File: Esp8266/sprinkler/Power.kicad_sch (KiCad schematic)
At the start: 54 parts, among them Q1 AO4407A, Q2 MMBT2222A, Q3 AON7410, U1 MAX1873TEEE, U2 TPS5410DR, U3 PC817, U4 LM2577S-ADJ_NOPB

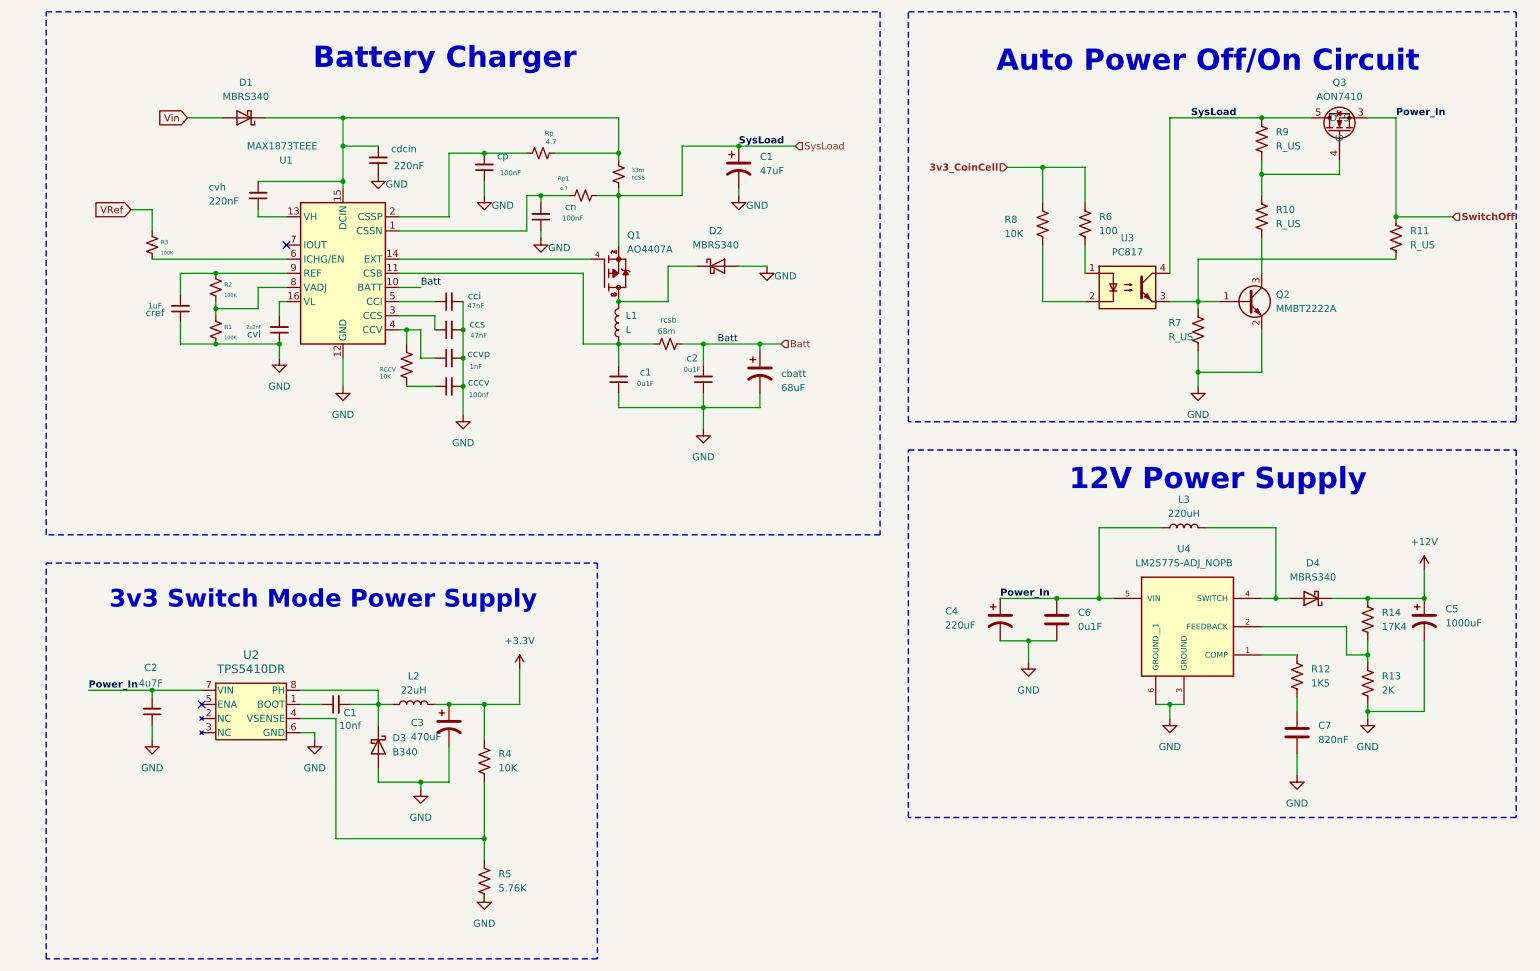
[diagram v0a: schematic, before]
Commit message: Sprinklers
Added RTC and valver drivers modules for the Sprinklers
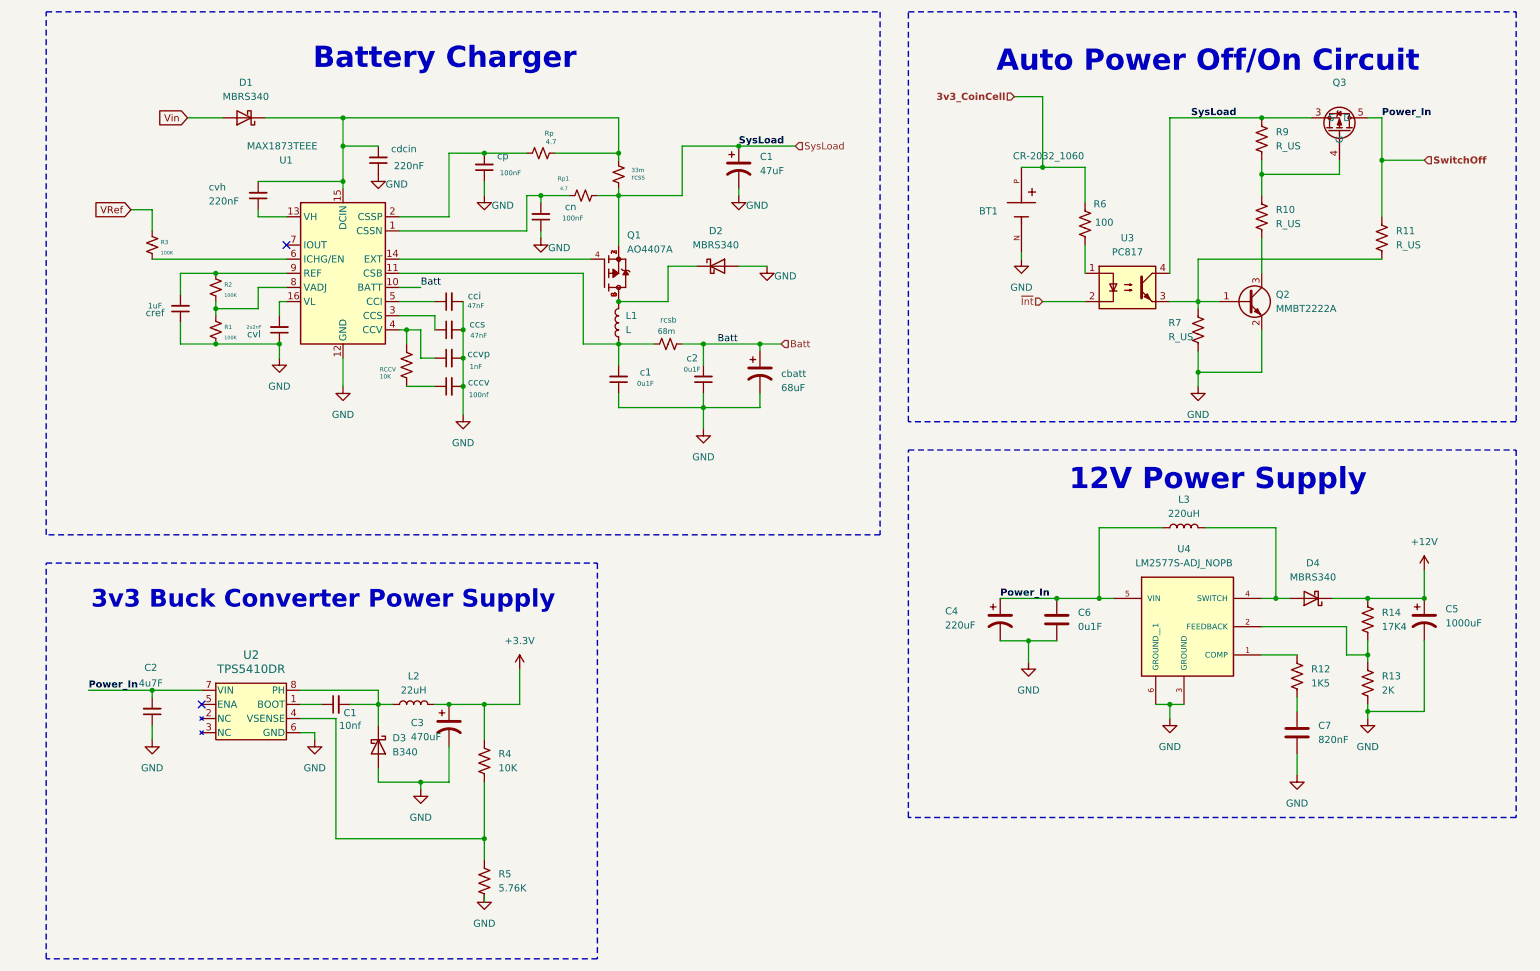
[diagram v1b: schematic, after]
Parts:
- removed Q3: AON7410, Local_Footprints:DFN_3X3_EP, symbol _Misc_Symbols:AON7410
- removed R8: 10K, symbol Device:R_US
- added BT1: CR-2032_1060, User_Footprint:BAT_1060, symbol _Misc_Symbols:CR-2032_1060
- added Q3: ~, User_Footprint:DFN_3X3_EP, symbol _Misc_Symbols:AON7401
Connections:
- net 3v3_CoinCell: now also BT1.P
- net GND: now also BT1.N
- net SwitchOff: now also Q3.5 (D), Q3.6 (D), Q3.7 (D), Q3.8 (D)
- net SysLoad: now also Q3.3 (S)
- net ~{Int}: now reaches U3.2
- net at R10.1, R9.2: now also Q3.4 (G)
- new net: Q3.1 (S), Q3.2 (S)
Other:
- note added: "3v3 Buck Converter Power Supply"
- note removed: "3v3 Switch Mode Power Supply"
- moved on the sheet: R11

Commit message: Transistor changes
Changed all Bjt transistors to Mosfets
Assign footprints
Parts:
- removed L1: L, symbol Device:L
- removed Q2: MMBT2222A, Package_TO_SOT_SMD:SOT-23, symbol Transistor_BJT:MMBT2222A
- added L2: CDRH105RNP-100NC, User_Footprint:IND_CDRH105RNP-100NC, symbol _Misc_Symbols:CDRH105RNP-100NC
- added Q2, Q3, Q5: 2N7002, Package_TO_SOT_SMD:SOT-23, symbol Transistor_FET:2N7002
- added R14: 1M, Resistor_SMD:R_0805_2012Metric_Pad1.20x1.40mm_HandSolder, symbol Device:R_US
- C1: renamed from C2; footprint (none) -> Capacitor_SMD:C_0805_2012Metric_Pad1.18x1.45mm_HandSolder
- C10: renamed from C5; footprint (none) -> User_Footprint:CAPAE1910X2250N; symbol Device:C_Polarized_US -> _Misc_Symbols:UUG1V102MNQ6MS; Height (none) -> 22.5; Manufacturer_Name (none) -> Nichicon; Manufacturer_Part_Number (none) -> UUG1V102MNQ6MS; Mouser Part Number (none) -> 647-UUG1V102MNQ6MS; Mouser Price/Stock (none) -> https://www.mouser.co.uk/ProductDetail/Nichicon/UUG1V102MNQ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
- C2: renamed from C1; footprint (none) -> Capacitor_SMD:C_0805_2012Metric_Pad1.18x1.45mm_HandSolder
- C3: footprint (none) -> Capacitor_SMD:CP_Elec_10x10
- C6: renamed from C1; footprint (none) -> Capacitor_Tantalum_SMD:CP_EIA-7343-31_Kemet-D_HandSolder
- C7: renamed from C4; footprint (none) -> Capacitor_Tantalum_SMD:CP_EIA-7360-38_Kemet-E_HandSolder
- C8: renamed from C6; footprint (none) -> Capacitor_SMD:C_0805_2012Metric_Pad1.18x1.45mm_HandSolder
- C9: renamed from C7; footprint (none) -> Capacitor_SMD:C_0805_2012Metric_Pad1.18x1.45mm_HandSolder
- L3: footprint (none) -> User_Footprint:SLF12575; symbol Device:L -> _Misc_Symbols:SLF12575T-221M1R3-H; Manufacturer_Name (none) -> TDK; Manufacturer_Part_Number (none) -> SLF12575T-221M1R3-H; Mouser Part Number (none) -> 810-SLF12575T221M1R3; Mouser Price/Stock (none) -> https://www.mouser.co.uk/ProductDetail/TDK/SLF12575T-221M1R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
- R1: renamed from R3; footprint (none) -> Resistor_SMD:R_0805_2012Metric_Pad1.20x1.40mm_HandSolder
- R10: renamed from R12; footprint (none) -> Resistor_SMD:R_0805_2012Metric_Pad1.20x1.40mm_HandSolder
- R11: value R_US -> 50K; footprint (none) -> Resistor_SMD:R_0805_2012Metric_Pad1.20x1.40mm_HandSolder
- R12: renamed from R14; footprint (none) -> Resistor_SMD:R_0805_2012Metric_Pad1.20x1.40mm_HandSolder
- R13, R2, R4, R5, R6: footprint (none) -> Resistor_SMD:R_0805_2012Metric_Pad1.20x1.40mm_HandSolder
- R3: renamed from R1; footprint (none) -> Resistor_SMD:R_0805_2012Metric_Pad1.20x1.40mm_HandSolder
- R7: value R_US -> 10K; footprint (none) -> Resistor_SMD:R_0805_2012Metric_Pad1.20x1.40mm_HandSolder
- R8: renamed from R9; value R_US -> 100K; footprint (none) -> Resistor_SMD:R_0805_2012Metric_Pad1.20x1.40mm_HandSolder
- R9: renamed from R10; value R_US -> 100K; footprint (none) -> Resistor_SMD:R_0805_2012Metric_Pad1.20x1.40mm_HandSolder
- RCCV1: renamed from RCCV; footprint (none) -> Resistor_SMD:R_0805_2012Metric_Pad1.20x1.40mm_HandSolder
- Rp1: renamed from Rp; footprint (none) -> Resistor_SMD:R_0805_2012Metric_Pad1.20x1.40mm_HandSolder
- Rp2: renamed from Rp1; footprint (none) -> Resistor_SMD:R_0805_2012Metric_Pad1.20x1.40mm_HandSolder
- U1: renamed from U2; footprint Local_Footprints:SOIC-8-1EP_3.9x4.9mm_P1.27mm -> User_Footprint:SOIC-8-1EP_3.9x4.9mm_P1.27mm
- c4: renamed from c1; footprint (none) -> Capacitor_SMD:C_0805_2012Metric_Pad1.18x1.45mm_HandSolder
- c5: renamed from c2; footprint (none) -> Capacitor_SMD:C_0805_2012Metric_Pad1.18x1.45mm_HandSolder
- cbatt1: renamed from cbatt; footprint (none) -> Capacitor_Tantalum_SMD:CP_EIA-7360-38_Kemet-E_HandSolder
- cccv1: renamed from cccv; footprint (none) -> Capacitor_SMD:C_0805_2012Metric_Pad1.18x1.45mm_HandSolder
- cci1: renamed from cci; footprint (none) -> Capacitor_SMD:C_0805_2012Metric_Pad1.18x1.45mm_HandSolder
- ccs1: renamed from ccs; footprint (none) -> Capacitor_SMD:C_0805_2012Metric_Pad1.18x1.45mm_HandSolder
- ccvp1: renamed from ccvp; footprint (none) -> Capacitor_SMD:C_0603_1608Metric_Pad1.08x0.95mm_HandSolder
- cdcin1: renamed from cdcin; footprint (none) -> Capacitor_SMD:C_0805_2012Metric_Pad1.18x1.45mm_HandSolder
- cn1: renamed from cn; footprint (none) -> Capacitor_SMD:C_0805_2012Metric_Pad1.18x1.45mm_HandSolder
- cp1: renamed from cp; footprint (none) -> Capacitor_SMD:C_0805_2012Metric_Pad1.18x1.45mm_HandSolder
- cref1: renamed from cref; footprint (none) -> Capacitor_SMD:C_0805_2012Metric_Pad1.18x1.45mm_HandSolder
- cvh1: renamed from cvh; footprint (none) -> Capacitor_SMD:C_0805_2012Metric_Pad1.18x1.45mm_HandSolder
- cvl1: renamed from cvl; footprint (none) -> Capacitor_SMD:C_0805_2012Metric_Pad1.18x1.45mm_HandSolder
- rcsb1: renamed from rcsb; footprint (none) -> Resistor_SMD:R_2512_6332Metric_Pad1.40x3.35mm_HandSolder
- rcss1: renamed from rcss; footprint (none) -> Resistor_SMD:R_2512_6332Metric_Pad1.40x3.35mm_HandSolder
- renumbered D3 to D2, D2 to D3, L2 to L1, Q3 to Q4, U1 to U2
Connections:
- net GND: now also Q3.2 (S), Q5.2 (S), R14.2
- net SwitchOff: now also Q5.1 (G), R14.1; no longer C1.2, C7.1, C8.1, L3.1, Q4.5 (D), Q4.6 (D), Q4.7 (D), Q4.8 (D), R11.1, U1.7 (VIN), U4.5 (VIN)
- net SysLoad: now also Q2.3 (D); no longer U3.4
- net at R11.2, R7.1, U3.3: now also Q3.1 (G), Q5.3 (D)
- net at R9.2: now also Q2.1 (G), Q3.3 (D)
- net at U2.11 (CSB), c4.2, rcsb1.1: now also L2.2
- net at D3.1 (K), Q1.5, Q1.6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: now also L2.1
- new net: Q2.2 (S), U3.4
- new net Power_In: C1.2, C7.1, C8.1, L3.1, Q4.5 (D), Q4.6 (D), Q4.7 (D), Q4.8 (D), R11.1, U1.7 (VIN), U4.5 (VIN)
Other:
- moved on the sheet: BT1, Q4, R11, R6, R7, R8, R9, U3, c4, c5, cbatt1, rcsb1

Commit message: Update connections
Connect Micro controller inputs and outputs
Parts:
- removed Q1: AO4407A, AO4407A:SOIC127P600X175-8N, symbol Alpha_Omega:AO4407A
- added D8: BAT54C, Package_TO_SOT_SMD:SOT-23, symbol Diode:BAT54C
- added J5, J6: Terminal Block 1729128, User_Footprint:CONN_1729128_PXC, symbol _Connectors:Terminal Block 1729128
- added Q9: AO4407A, User_Footprint:SOIC127P600X175-8N, symbol _Misc_Symbols:AO4407A
- added S1: TS04-66-70-BK-260-SMT, User_Footprint:SW_TS04-66-70-BK-260-SMT, symbol _Misc_Symbols:TS04-66-70-BK-260-SMT
- C1, C2, C3, D2, L1, R4, R5: now not fitted
- Q4: value ~ -> AON7401
- U1: footprint User_Footprint:SOIC-8-1EP_3.9x4.9mm_P1.27mm -> Local_Footprints:SOIC-8-1EP_3.9x4.9mm_P1.27mm; now not fitted
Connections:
- net Batt: now also J5.1
- net GND: now also J5.2, J6.1, S1.2, S1.4
- net Power_In: no longer C1.2, Q4.5 (D), Q4.6 (D), Q4.7 (D), Q4.8 (D), R11.1, U1.7 (VIN)
- net SysLoad: now also Q4.1 (S), Q4.2 (S), Q9.1, Q9.2, Q9.3
- net ~{Int}: now also S1.1, S1.3
- net at D3.1 (K), L2.1: now also Q9.5, Q9.6, Q9.7, Q9.8
- net at U2.14 (EXT): now also Q9.4
- net +3.3V: no longer names the net of C3.1, L1.2, R4.1
- net 3v3_CoinCell: no longer names the net of BT1.P
- net 3v3_CoinCell: now also D8.2; no longer R6.1
- net Vin: no longer names the net of D1.2 (A)
- net Vin: now also J6.2
- new net 3V3: D8.3, R6.1
- new net PowerIn: C1.2, Q4.5 (D), Q4.6 (D), Q4.7 (D), Q4.8 (D), R11.1, U1.7 (VIN)
- new net esp8266_3V3: D8.1
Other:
- moved on the sheet: BT1

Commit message: pcb
First component layout (need to verify ESP8266 board size for fitment)
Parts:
- added TP10, TP9: TestPoint, TestPoint:TestPoint_Pad_1.0x1.0mm, symbol Connector:TestPoint
- J1: renamed from J6; footprint User_Footprint:CONN_1729128_PXC -> User_Footprint:OQ0212500000G; symbol _Connectors:Terminal Block 1729128 -> _Connectors:OQ0212500000G; Height (none) -> 9.2; Manufacturer_Name (none) -> Amphenol; Manufacturer_Part_Number (none) -> OQ0212500000G; Mouser Part Number (none) -> 649-220107-C021A01LF; Mouser Price/Stock (none) -> https://www.mouser.co.uk/ProductDetail/Amphenol-Anytek/OQ02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
- J2: renamed from J5; footprint User_Footprint:CONN_1729128_PXC -> User_Footprint:OQ0212500000G; symbol _Connectors:Terminal Block 1729128 -> _Connectors:OQ0212500000G; Height (none) -> 9.2; Manufacturer_Name (none) -> Amphenol; Manufacturer_Part_Number (none) -> OQ0212500000G; Mouser Part Number (none) -> 649-220107-C021A01LF; Mouser Price/Stock (none) -> https://www.mouser.co.uk/ProductDetail/Amphenol-Anytek/OQ02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
- renumbered cvl1 to C1, C2 to C10, C3 to C11, C7 to C12, ccvp1 to C13, c5 to C14, c4 to C15, cref1 to C16, C8 to C17, C9 to C18, C10 to C19, cvh1 to C2, cdcin1 to C3, cci1 to C4, ccs1 to C5, cccv1 to C6, cp1 to C7, cn1 to C8, C1 to C9, cbatt1 to CBAT1, C6 to CL1, D3 to D2, D2 to D3, D8 to D4, D4 to D5, L2 to L1, L1 to L2, Q9 to Q1, rcss1 to R1, R5 to R10, R6 to R11, R7 to R12, R8 to R13, R9 to R14, R10 to R15, R11 to R16, R12 to R17, R13 to R18, R14 to R19, rcsb1 to R2, R2 to R3, R3 to R4, RCCV1 to R5, Rp1 to R6, Rp2 to R7, R1 to R8, R4 to R9, U2 to U1, U1 to U2
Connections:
- net +12V: now also TP10.1
- net GND: now also J2.1; no longer J2.2
- net SysLoad: now also TP9.1
- net SolarPower: now reaches D1.2 (A), J1.2
- net Batt: no longer names the net of C14.2, CBAT1.1, R2.2, U1.10 (BATT)
- net Batt: now also J2.2; no longer J2.1
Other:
- moved on the sheet: C14, C15, CBAT1, CL1, D2, R2

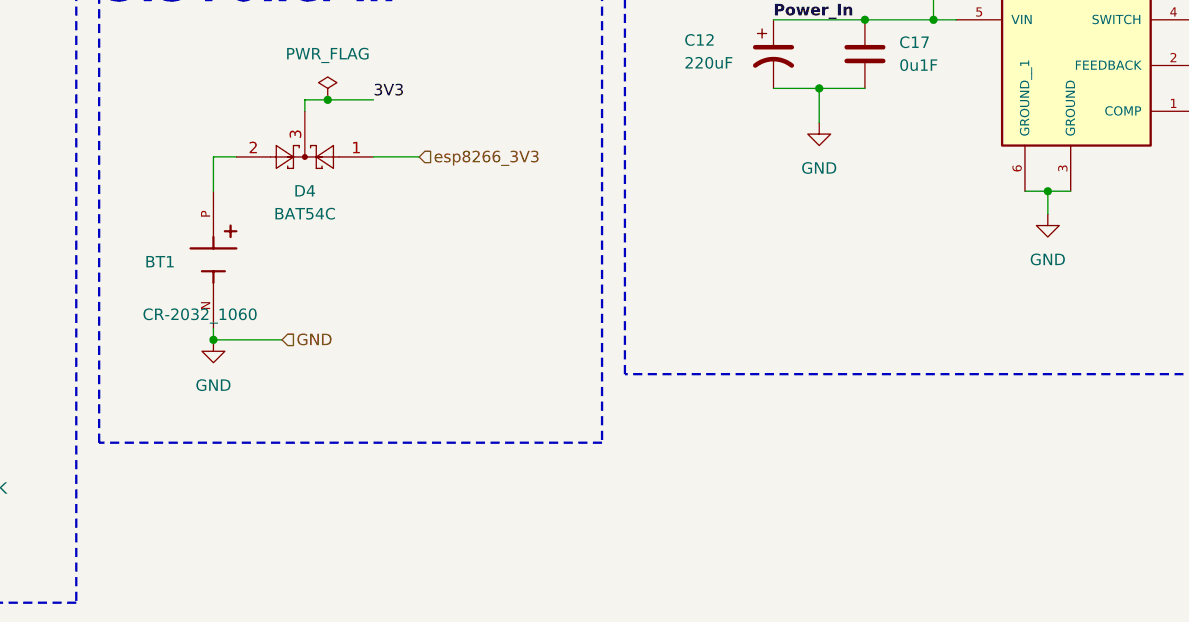
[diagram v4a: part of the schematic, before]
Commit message: holes
Adding mounting holes
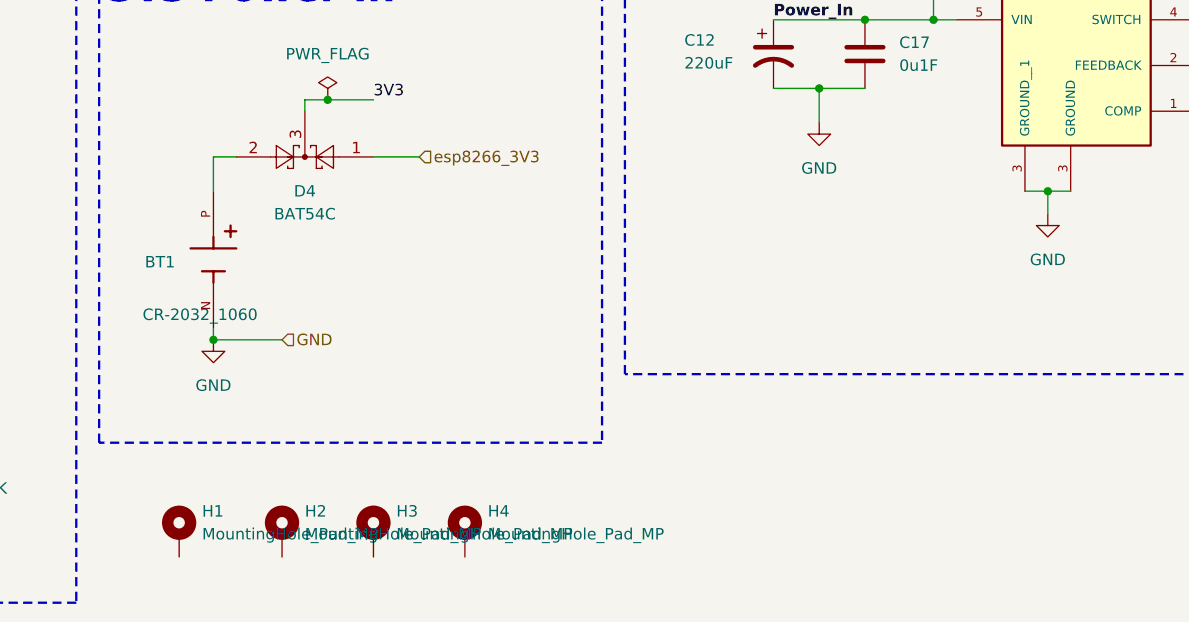
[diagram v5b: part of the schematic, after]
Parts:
- added H1, H2, H3, H4: MountingHole_Pad_MP, MountingHole:MountingHole_2.7mm_Pad_Via, symbol Mechanical:MountingHole_Pad_MP
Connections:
- net GND: no longer U4.6 (GROUND__1)
